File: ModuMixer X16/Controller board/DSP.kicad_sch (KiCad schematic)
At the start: 51 parts, among them Q3 MMBT2222A, Q4 MMBT2222A, U11 LM358, U5 LM324, U6 AMS1117-1.8, U7 TLV320AIC3100, U8 STM32F405RGTx, U9 4016

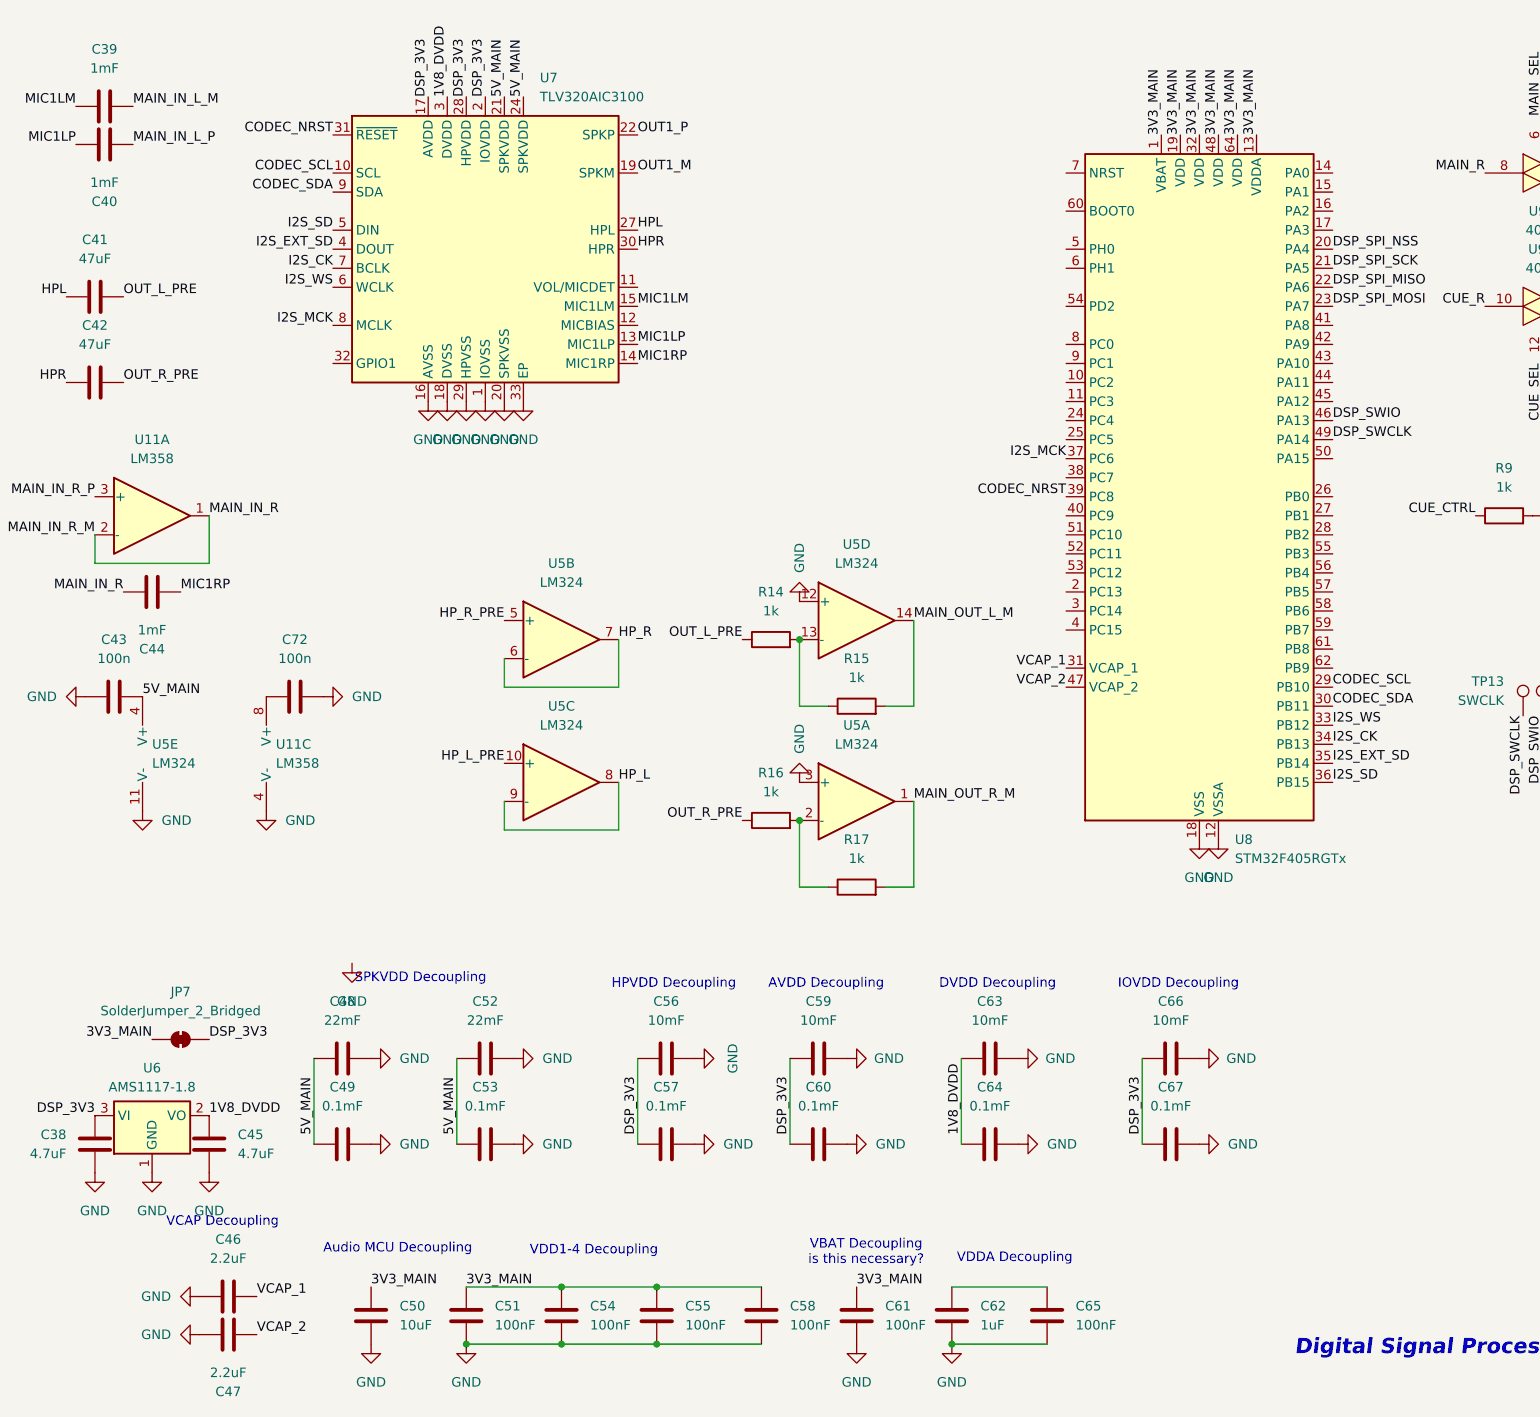
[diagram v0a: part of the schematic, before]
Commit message: Switching microcontrollers
Midway through switching all microcontrollers in the project to STM32F103RC due to price constraints
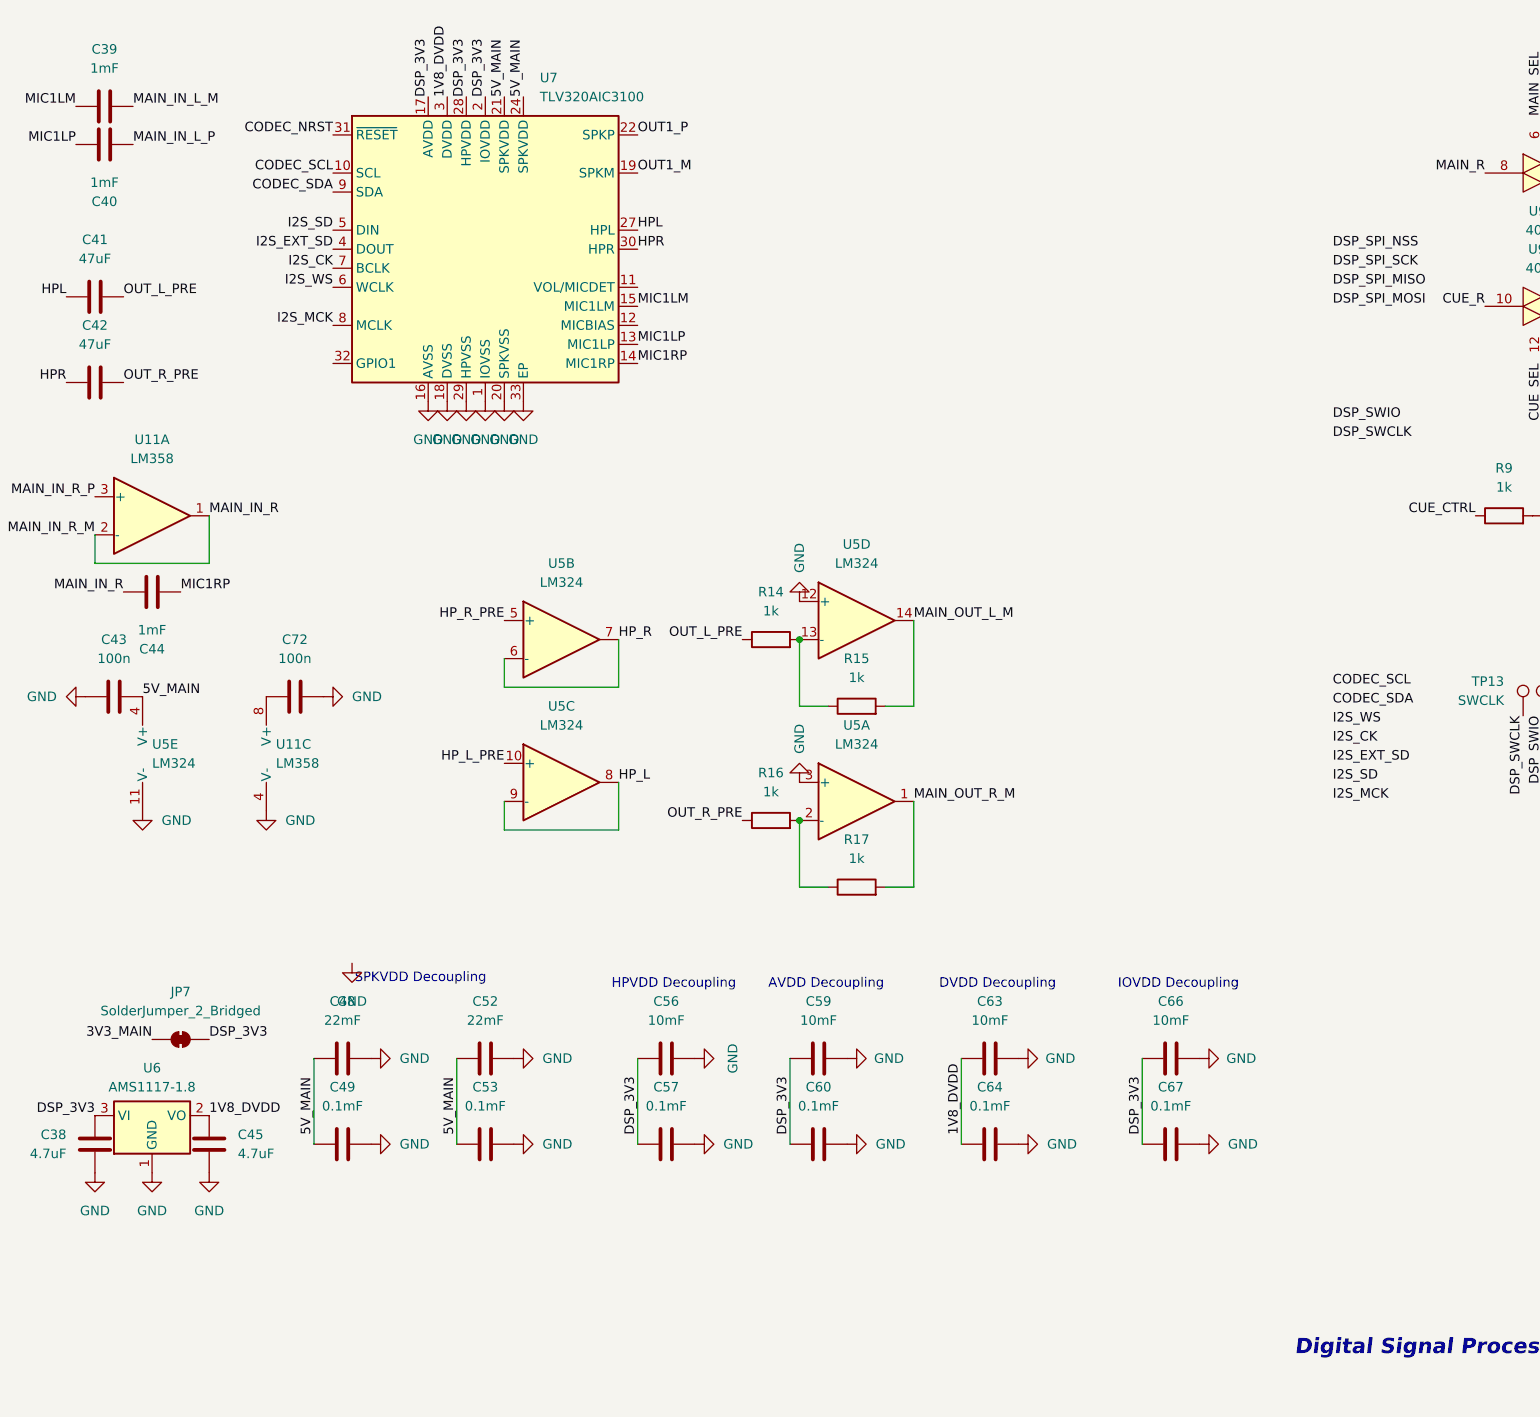
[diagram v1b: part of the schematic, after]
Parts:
- removed C46, C47: 2.2uF, Capacitor_SMD:C_0603_1608Metric, symbol Device:C
- removed C50: 10uF, Capacitor_SMD:C_0603_1608Metric, symbol Device:C
- removed C51, C54, C55, C58, C61, C65: 100nF, Capacitor_SMD:C_0603_1608Metric, symbol Device:C
- removed C62: 1uF, Capacitor_SMD:C_0603_1608Metric, symbol Device:C
- removed U8: STM32F405RGTx, Package_QFP:LQFP-64_10x10mm_P0.5mm, symbol MCU_ST_STM32F4:STM32F405RGTx
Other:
- note removed: "Audio MCU Decoupling"
- note removed: "VBAT Decoupling is this necessary?"
- note removed: "VCAP Decoupling"
- note removed: "VDD1-4 Decoupling"
- note removed: "VDDA Decoupling"

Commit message: Midway through MCU replacement
Sometimes i feel like it would be better to start over considering it's a digital mixer.
The only thing left is doing the DSP connections and calculating the values for a 16mhz crystal on all 3 MCUs
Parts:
- added U10: STM32F103RCTx, Package_QFP:LQFP-64_10x10mm_P0.5mm, symbol MCU_ST_STM32F1:STM32F103RCTx
- renumbered C41 to C18, C42 to C19, C38 to C20, C39 to C21, C40 to C22, C43 to C23, C44 to C24, C45 to C25, C72 to C26, C48 to C27, C49 to C28, C52 to C29, C53 to C30, C56 to C31, C57 to C32, C59 to C33, C60 to C34, C63 to C35, C64 to C36, C66 to C37, C67 to C38, C68 to C39, JP7 to JP4, R16 to R10, R15 to R11, R17 to R12, R9 to R13, R10 to R14, R11 to R15, R12 to R16, R14 to R9, TP13 to TP8, TP14 to TP9, U9 to U11, U11 to U6, U6 to U7, U5 to U8, U7 to U9
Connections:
- net DSP_SWCLK: now also U10.49 (PA14)
- net DSP_SWIO: now also U10.46 (PA13)
- new net: U10.18 (VSS), U10.31 (VSS), U10.47 (VSS), U10.63 (VSS)
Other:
- moved on the sheet: TP8, TP9

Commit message: MCU replacement done
I finally did everything (i guess), i replaced the MCUs, set the clock components, connected them, idk i guess it's ok now, we just gotta make that pcb
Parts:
- removed TP8: SWCLK, TestPoint:TestPoint_Pad_D3.0mm, symbol Connector:TestPoint
- removed TP9: SWIO, TestPoint:TestPoint_Pad_D3.0mm, symbol Connector:TestPoint
- added C49, C50: 30pF, symbol Device:C
- added C61, C62, C63, C64: 100nF, symbol Device:C
- added C65: 1uF, symbol Device:C
- added R22: 1M, symbol Device:R
- added Y4: 16MHz, Crystal:Crystal_HC49-U_Vertical, symbol Device:Crystal
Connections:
- net CODEC_SCL: now also U10.29 (PB10)
- net CODEC_SDA: now also U10.30 (PB11)
- net CUE_CTRL: now also U10.14 (PA0)
- net DSP_3V3: now also U10.13 (VDDA), U10.19 (VDD), U10.32 (VDD), U10.48 (VDD), U10.64 (VDD), C61.1, C62.1, C63.1, C64.1, C65.1
- net DSP_SPI_MISO: now also U10.22 (PA6)
- net DSP_SPI_MOSI: now also U10.23 (PA7)
- net DSP_SPI_NSS: now also U10.20 (PA4)
- net DSP_SPI_SCK: now also U10.21 (PA5)
- net GND: now also U10.12 (VSSA), U10.18 (VSS), U10.31 (VSS), U10.47 (VSS), U10.63 (VSS), C49.2, C50.2, C61.2, C62.2, C63.2, C64.2, C65.2
- net I2S_CK: now also U10.34 (PB13)
- net I2S_EXT_SD: now also U10.35 (PB14)
- net I2S_MCK: now also U10.37 (PC6)
- net I2S_SD: now also U10.36 (PB15)
- net I2S_WS: now also U10.33 (PB12)
- net DSP_CLK1: now reaches U10.5 (PD0)
- net DSP_CLK1: now also C49.1, R22.1, Y4.2
- net DSP_CLK2: now reaches U10.6 (PD1)
- net DSP_CLK2: now also C50.1, R22.2, Y4.1
- net DSP_BOOT: now reaches U10.60 (BOOT0)
- net DSP_RESET: now reaches U10.7 (NRST)
- net DSP_SWCLK renamed DSP_SWDCLK
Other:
- moved on the sheet: U10

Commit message: asdasgashg
sfjhadgdjasdg
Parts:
- C55: renamed from C49; footprint (none) -> Capacitor_SMD:C_0603_1608Metric
- C56: renamed from C50; footprint (none) -> Capacitor_SMD:C_0603_1608Metric
- C57: renamed from C65; footprint (none) -> Capacitor_SMD:C_0603_1608Metric
- C58: renamed from C61; footprint (none) -> Capacitor_SMD:C_0603_1608Metric
- C59: renamed from C62; footprint (none) -> Capacitor_SMD:C_0603_1608Metric
- C61: renamed from C63; footprint (none) -> Capacitor_SMD:C_0603_1608Metric
- C62: renamed from C64; footprint (none) -> Capacitor_SMD:C_0603_1608Metric
- R18: renamed from R22; footprint (none) -> Resistor_SMD:R_0603_1608Metric
- renumbered C18 to C34, C19 to C35, C20 to C36, C21 to C37, C22 to C38, C23 to C39, C24 to C40, C25 to C41, C26 to C42, C27 to C43, C28 to C44, C29 to C45, C30 to C46, C31 to C47, C32 to C48, C33 to C49, C34 to C50, C35 to C51, C36 to C52, C37 to C53, C38 to C54, C39 to C60, JP4 to JP5, Q3 to Q4, Q4 to Q5, R9 to R13, R10 to R14, R11 to R15, R12 to R16, R13 to R17, R14 to R19, R15 to R20, R16 to R21

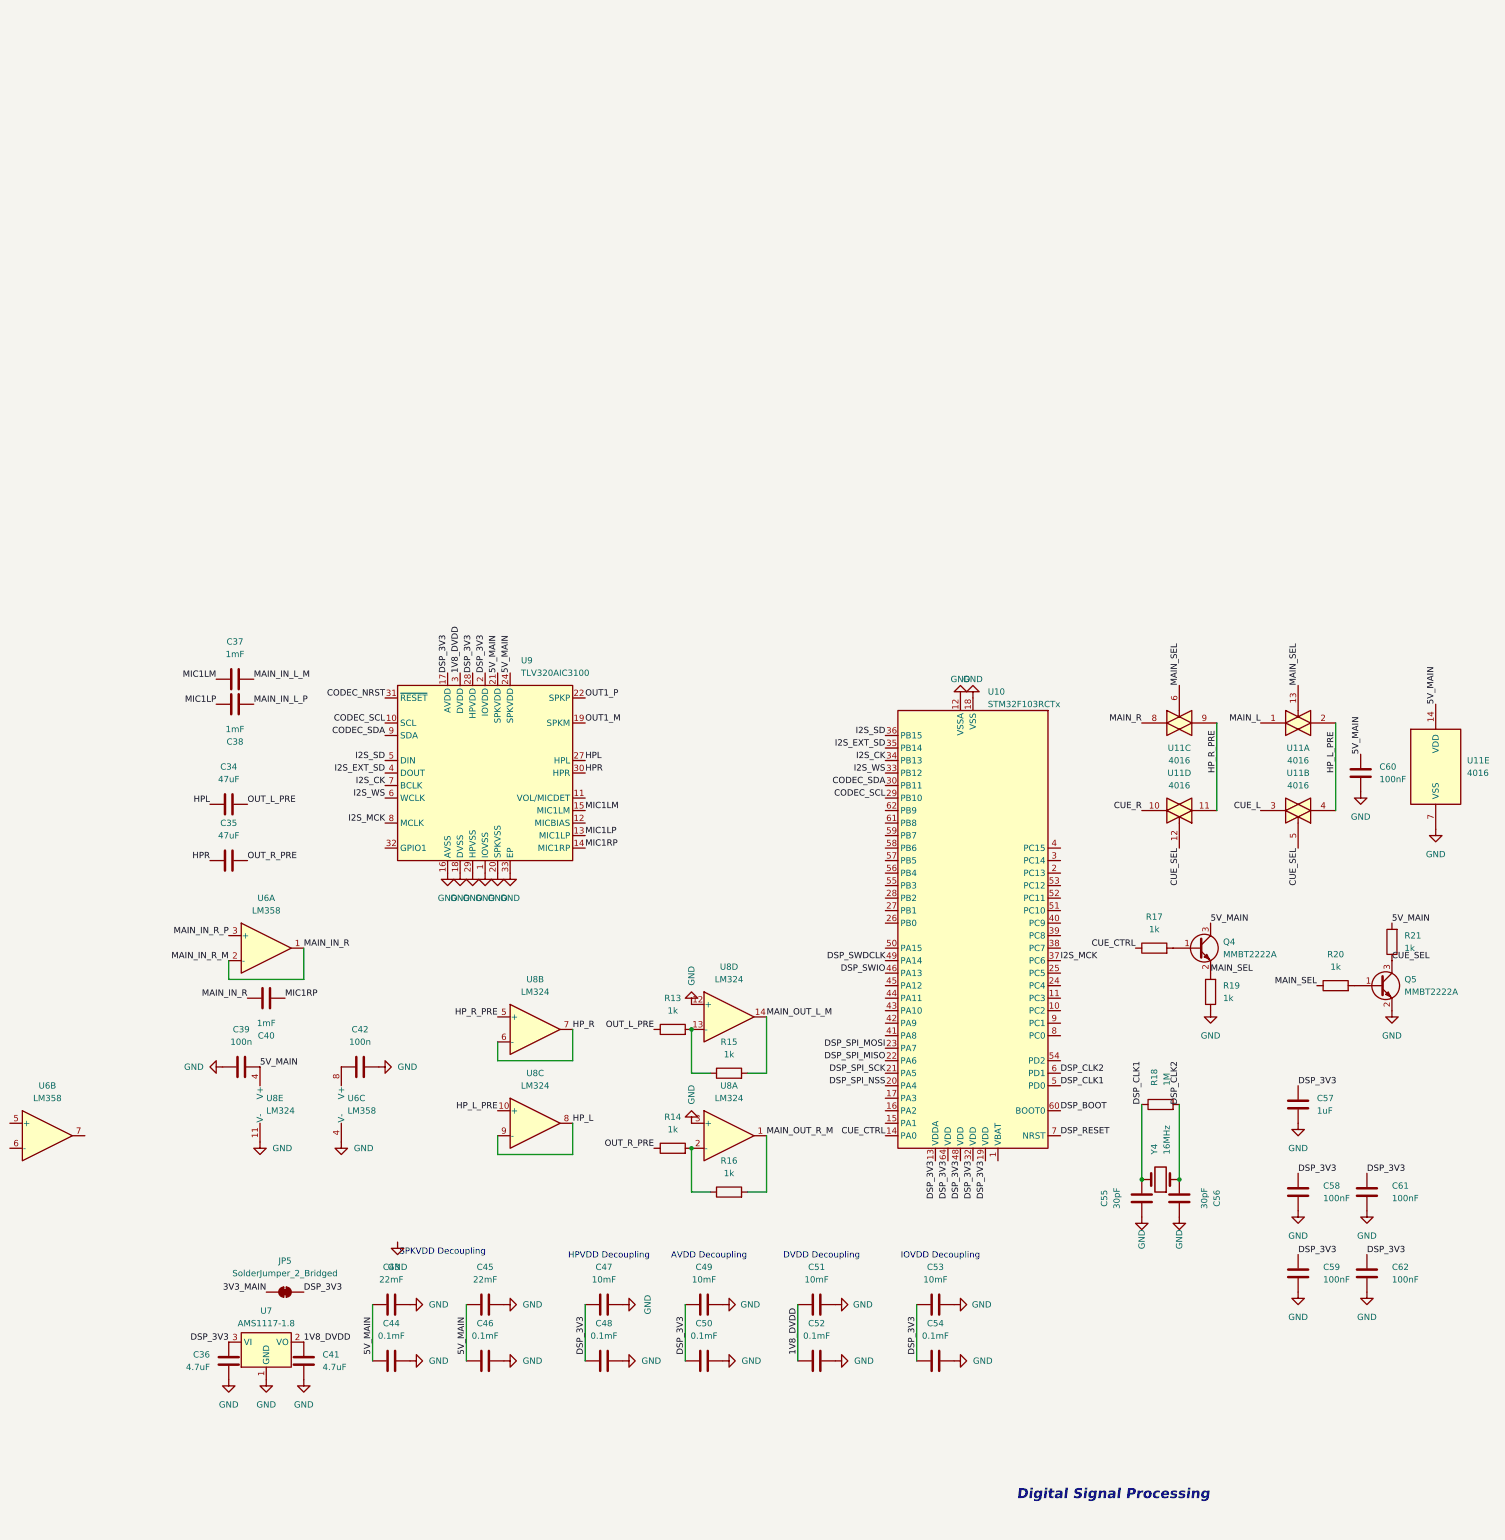
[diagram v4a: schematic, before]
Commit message: Changed all labels to global
I made it in a rather hacky way (editing all files on notepad with Ctrl + H), i'm only reverting this if something breaks
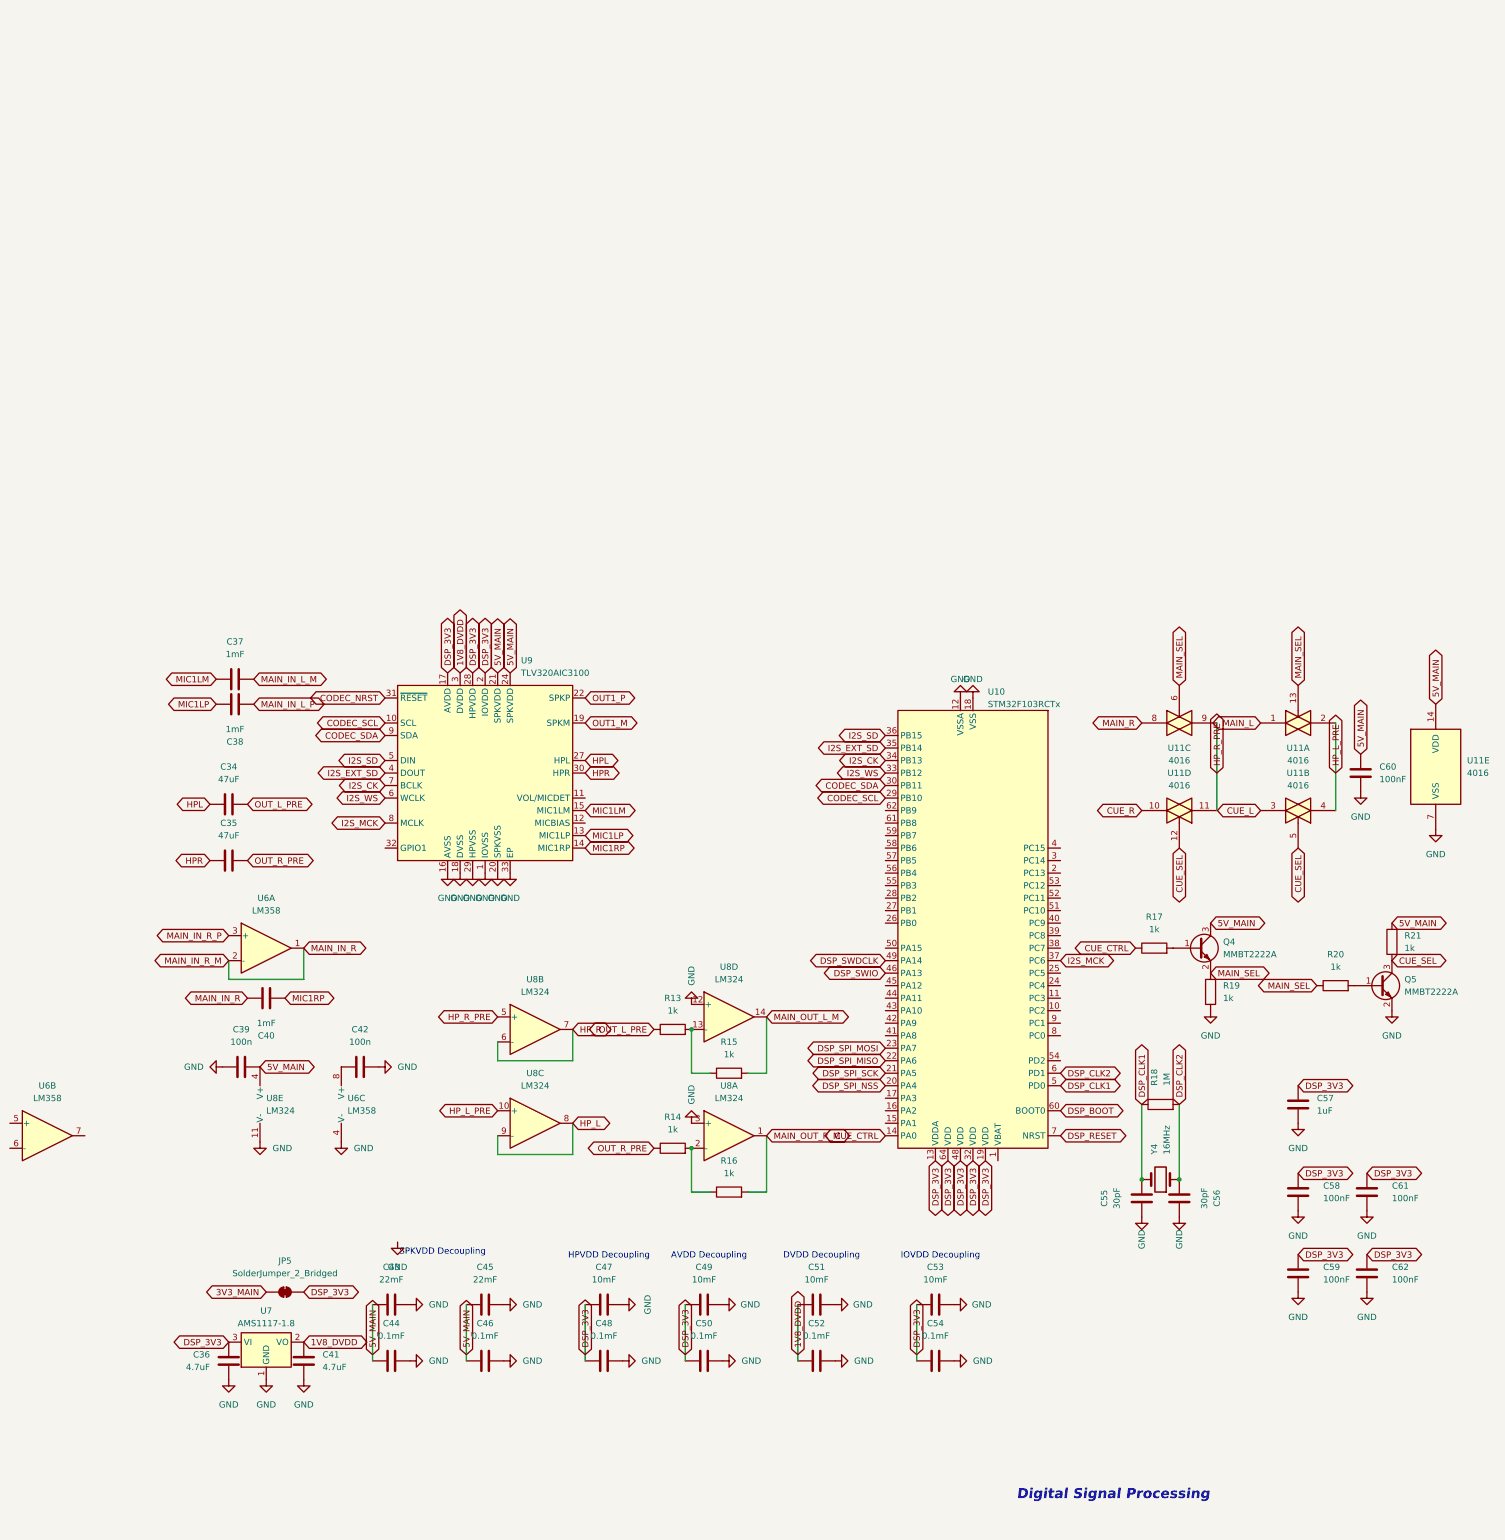
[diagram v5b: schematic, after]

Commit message: MCU replacement finished
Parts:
- added R27, R28: 1k, Resistor_SMD:R_0603_1608Metric, symbol Device:R
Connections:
- net DSP_3V3: now also R28.1
- net DSP_BOOT: now also R27.2, R28.2
- net GND: now also R27.1
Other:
- moved on the sheet: U8B, U8C
